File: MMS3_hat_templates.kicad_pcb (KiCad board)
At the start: 4 copper layers, 100 x 50 mm, 166 parts, among them J1 Chainbus in, J10 LED connector, J11 LED connector, J2 Chainbus Out, J3 Conn_01x04_Pin, J4 AMASS XT60 Male, J5 AMASS XT60 Female, J6 LED connector, J7 Conn_01x03_Pin, J9 Program, Q1 AO3400A, Q10 MMBT2222A 1P, Q11 MMBT2222A 1P, Q12 MMBT5401 200-300, Q13 AO3400A, Q14 MMBT2222A 1P, Q15 MMBT2222A 1P, Q16 MMBT5401 200-300, Q17 AO3400A, Q18 AO3400A, Q19 MMBT2222A 1P, Q2 MMBT2222A 1P, Q20 MMBT2222A 1P, Q21 MMBT5401 200-300, Q22 MMBT2222A 1P, Q23 MMBT2222A 1P, Q24 MMBT5401 200-300, Q25 2N7002K, Q26 2N7002K, Q27 AO3400A, Q28 MMBT2222A 1P, Q29 MMBT2222A 1P, Q3 MMBT2222A 1P, Q30 MMBT5401 200-300, Q31 AO3400A, Q32 AO3400A, Q33 MMBT2222A 1P, Q34 MMBT2222A 1P, Q35 MMBT5401 200-300, Q36 MMBT2222A 1P, Q37 MMBT2222A 1P, Q38 MMBT5401 200-300, Q4 MMBT5401 200-300, Q5 AO3400A, Q6 AO3400A, Q7 MMBT2222A 1P, Q8 MMBT2222A 1P, Q9 MMBT5401 200-300, U1 AMS1117, U2 SN74CB3Q3384APW, U3 M24C64, U4 PCA9685PW,118, U6 LM2596HVS-ADJRG, U7 CH32V003FxPx, X1 X322525MOB4SI

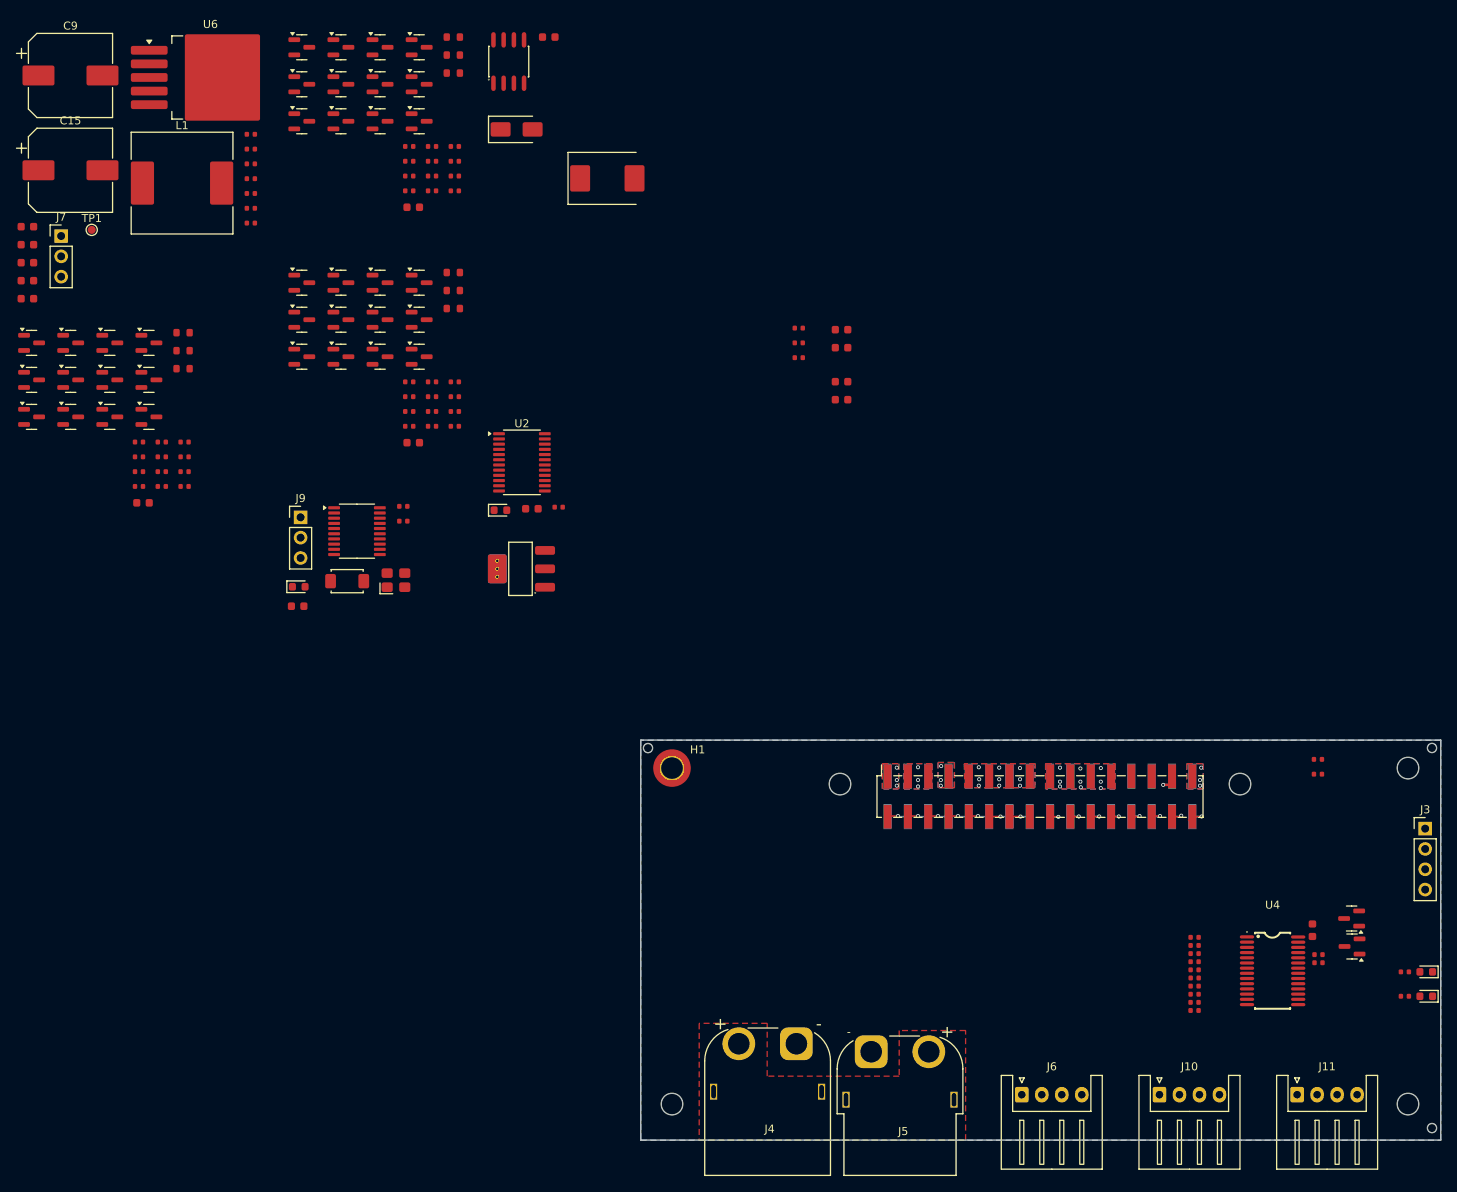
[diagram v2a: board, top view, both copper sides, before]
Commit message: PCB design
Hat allows to connect 1 LED tape at a time
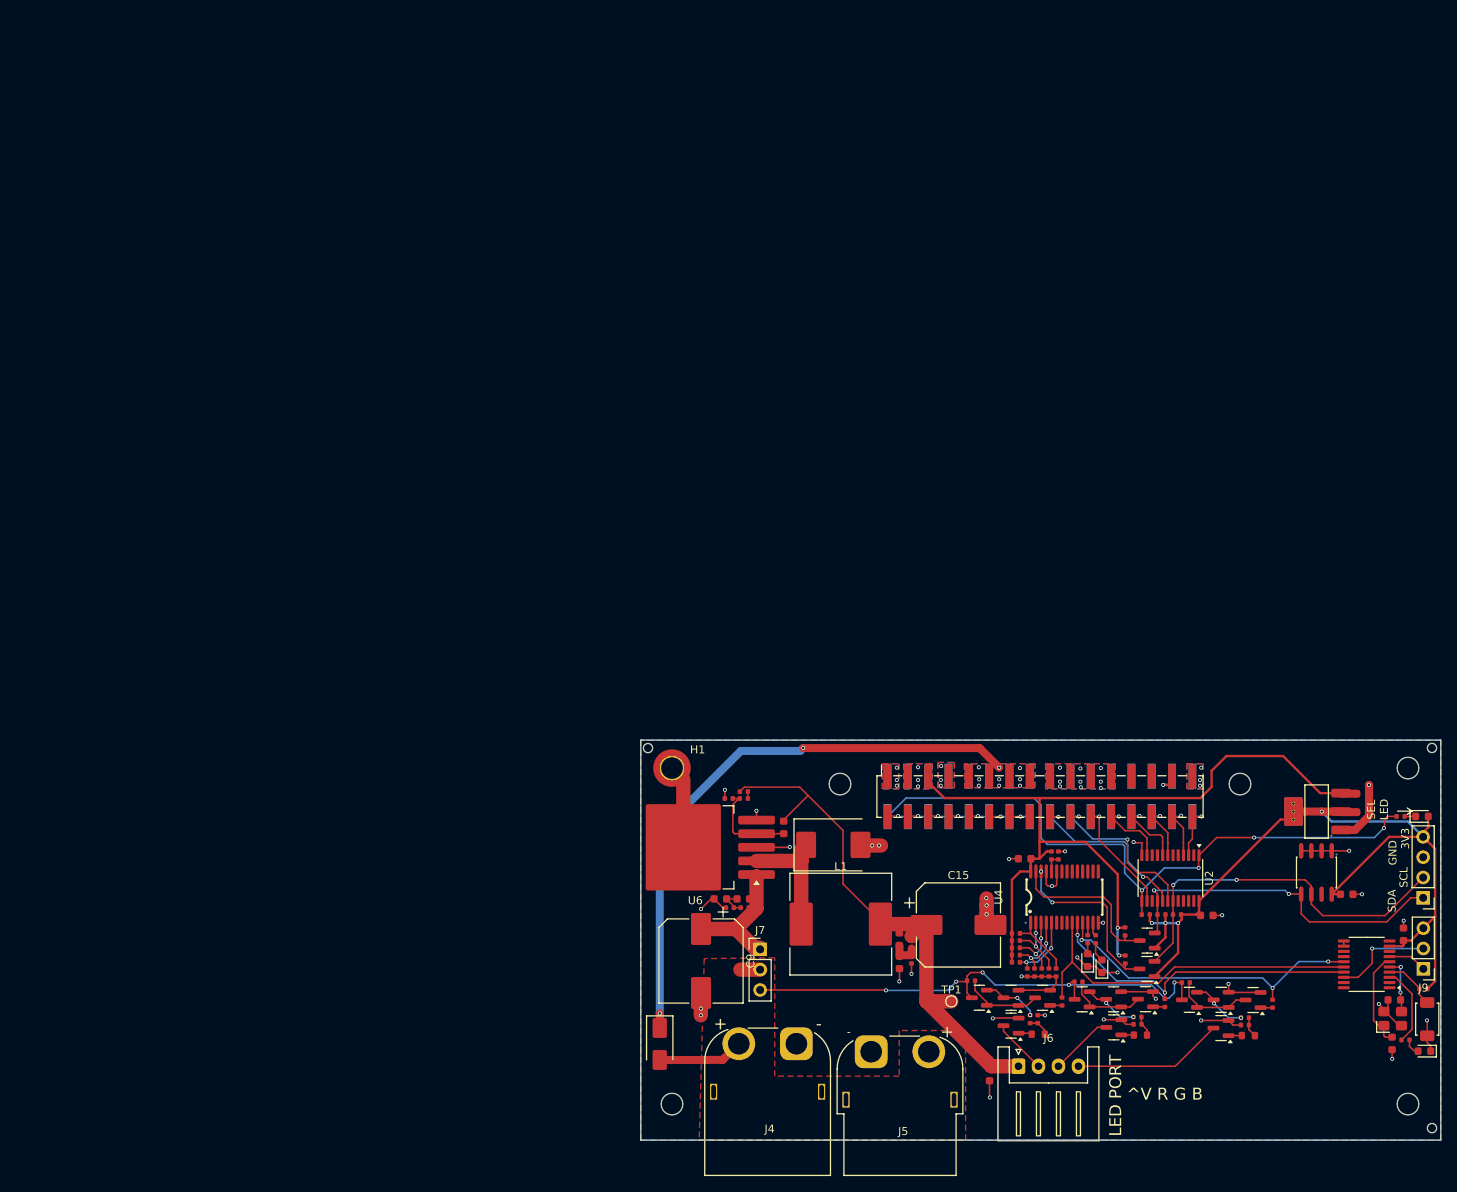
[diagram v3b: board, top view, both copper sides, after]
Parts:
- removed C19, C20: 100nF, PCM_JLCPCB:C_0603
- removed J10, J11: LED connector, Connector_JST:JST_XH_S4B-XH-A_1x04_P2.50mm_Horizontal
- removed Q14, Q15, Q19, Q20, Q22, Q23, Q28, Q29, Q33, Q34, Q36, Q37: MMBT2222A 1P, PCM_JLCPCB:Q_SOT-23
- removed Q16, Q21, Q24, Q30, Q35, Q38: MMBT5401 200-300, PCM_JLCPCB:Q_SOT-23
- removed Q17, Q18, Q31, Q32, Q5, Q6: AO3400A, PCM_JLCPCB:Q_SOT-23
- removed R34, R55, R58, R75, R78, R81: 100Ω, PCM_JLCPCB:R_0603
- removed R35, R53, R59, R73, R79, R82: 10kΩ, PCM_JLCPCB:R_0402
- removed R54, R63, R67, R74, R83, R87: 1kΩ, PCM_JLCPCB:R_0402
- removed R57, R65, R69, R77, R85, R89: 330Ω, PCM_JLCPCB:R_0402
- removed R60, R66, R70, R80, R86, R90: 47Ω, PCM_JLCPCB:R_0402
- moved Q10 158.2 mm to (154.6, 121.0), turned to 180 degrees
- moved R61 156.1 mm to (154.1, 125.4), turned to 180 degrees
- moved Q12 155.7 mm to (150.6, 121.0), turned to 180 degrees
- moved Q7 152.3 mm to (141.2, 120.9), turned to 180 degrees
- moved D9 152.2 mm to (176.0, 127.4), turned to 180 degrees
- moved Q27 151.3 mm to (150.6, 124.5), turned to 180 degrees
- moved J9 151.3 mm to (175.9, 117.1), turned to 180 degrees
- moved Q1 151.1 mm to (124.4, 124.2), turned to 180 degrees
- moved Q9 150.2 mm to (137.2, 120.9), turned to 180 degrees
- moved R31 149.6 mm to (140.6, 125.4), turned to 180 degrees
- moved Q11 149.3 mm to (146.7, 121.0), turned to 180 degrees
- moved R40 148.1 mm to (157.1, 121.5), turned to -90 degrees
- moved Q2 147.0 mm to (128.3, 120.7), turned to 180 degrees
- moved Q13 146.4 mm to (137.2, 124.4), turned to 180 degrees
- moved C4 146.4 mm to (166.3, 107.8)
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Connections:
- C12 pad 2: /12V -> U_reg
- C13 pad 1: /12V -> U_reg
- C15 pad 1: /12V -> U_reg
- J1 pad 18: /Interboard_connector/Chainbus.SDA -> /Bus_switch/Chainbus_In.SDA
- J1 pad 20: /Interboard_connector/Chainbus.SCL -> /Bus_switch/Chainbus_In.SCL
- J1 pad 22: /Interboard_connector/Chainbus.CS -> /Bus_switch/Chainbus_In.CS
- J1 pad 24: /Interboard_connector/Chainbus.SCK -> /Bus_switch/Chainbus_In.SCK
- J1 pad 26: /Interboard_connector/Chainbus.MOSI -> /Bus_switch/Chainbus_In.MOSI
- J1 pad 28: /Interboard_connector/Chainbus.MISO -> /Bus_switch/Chainbus_In.MISO
- J1 pad 30: /Interboard_connector/Chainbus.TX -> /Bus_switch/Chainbus_In.TX
- J1 pad 32: /Interboard_connector/Chainbus.RX -> /Bus_switch/Chainbus_In.RX
- J2 pad 18: /Interboard_connector/Chainbus.SDA -> /Bus_switch/Chainbus_In.SDA
- J2 pad 20: /Interboard_connector/Chainbus.SCL -> /Bus_switch/Chainbus_In.SCL
- J2 pad 22: /Interboard_connector/Chainbus.CS -> /Bus_switch/Chainbus_In.CS
- J2 pad 24: /Interboard_connector/Chainbus.SCK -> /Bus_switch/Chainbus_In.SCK
- J2 pad 26: /Interboard_connector/Chainbus.MOSI -> /Bus_switch/Chainbus_In.MOSI
- J2 pad 28: /Interboard_connector/Chainbus.MISO -> /Bus_switch/Chainbus_In.MISO
- J2 pad 30: /Interboard_connector/Chainbus.TX -> /Bus_switch/Chainbus_In.TX
- J2 pad 32: /Interboard_connector/Chainbus.RX -> /Bus_switch/Chainbus_In.RX
- L1 pad 2: /12V -> U_reg
- Q25 pad 2: /LED_IC/Chainbus.SCL -> /Bus_switch/Chainbus.SCL
- Q26 pad 2: /LED_IC/Chainbus.SDA -> /Bus_switch/Chainbus.SDA
- R48 pad 2: /12V -> U_reg
- R49 pad 1: /12V -> U_reg
- TP1 pad 1: /12V -> U_reg
- U3 pad 5: /ID EEPROM/Chainbus.SDA -> /Bus_switch/Chainbus.SDA
- U3 pad 6: /ID EEPROM/Chainbus.SCL -> /Bus_switch/Chainbus.SCL
- U4 pad 12: /R3 -> /LED_IC/S15
- U4 pad 13: /G3 -> /LED_IC/S16
- U4 pad 15: /B3 -> /LED_IC/LED8
- U4 pad 6: /R1 -> /LED_IC/LED0
- U4 pad 7: /G1 -> /LED_IC/LED1
- U4 pad 8: /B1 -> /LED_IC/LED2
- U7 pad 12: /Chainbus.SCL -> /Chainbus.SDA
- U7 pad 13: /R3 -> /CH32V003/PC3
- U7 pad 14: /G3 -> /CH32V003/PC4
- U7 pad 15: /B3 -> /B2
- U7 pad 8: /B2 -> /CH32V003/PD0
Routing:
- net GND: track 0.00 -> 116.4 mm, vias 18 -> 54
- net +5V: track 0.69 -> 109.0 mm, vias 3 -> 5
- net +3V3: track 0.00 -> 106.0 mm, vias 0 -> 4
- net /Bus_switch/SEL1: track 0.00 -> 82.1 mm, vias 0 -> 4
- net VIN_CHAINBUS: track 0.76 -> 73.0 mm, vias 9 -> 11
- net U_reg: track 0.00 -> 67.7 mm
- net /12V: track 0.00 -> 64.5 mm, vias 0 -> 5
- net /Bus_switch/Chainbus.SCL: track 0.00 -> 47.2 mm, vias 0 -> 2
- net /R2: track 0.00 -> 45.7 mm
- net /Bus_switch/Chainbus.SDA: track 0.00 -> 44.5 mm, vias 0 -> 2
- net /G2: track 0.00 -> 41.0 mm, vias 0 -> 2
- net /B2: track 0.00 -> 40.3 mm, vias 0 -> 3
- net /LED_IC/SCL_5V: track 0.00 -> 22.6 mm, vias 0 -> 2
- net /Bus_switch/Chainbus_In.SDA: track 0.00 -> 22.3 mm, vias 0 -> 2
- net /Bus_switch/Chainbus_In.SCL: track 0.00 -> 21.6 mm, vias 0 -> 2
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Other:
- board text added: "3V3"
- board text added: "GND"
- board text added: "LED PORT"
- board text added: "LED TAPE CONTROLLER HAT"
- board text added: "PWM CONTROLLER SETUP"
- board text added: "SCL"
- board text added: "SDA"
- board text added: "SEL LED"
- board text added: "^V R G B"
- board text added: "uC SETUP"

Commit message: PCB addjustments
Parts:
- added D10: SS510C, PCM_JLCPCB:D_SMC, F.Cu at (114.7, 119.6)
- added D8: SS510C, PCM_JLCPCB:D_SMC, F.Cu at (101.7, 120.2)
- moved TP1 5.40 mm to (119.0, 116.2)
- moved C15 3.84 mm to (118.0, 107.8)
- moved C13 3.51 mm to (110.3, 109.9)
- moved C14 3.51 mm to (110.4, 112.8)
- moved R49 3.51 mm to (111.9, 110.5)
- moved R50 3.51 mm to (111.9, 112.4)
- moved D6 1.25 mm to (102.1, 100.4)
- moved L1 1.23 mm to (102.9, 110.3)
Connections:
- C12 pad 2: U_reg -> Net-(C12-Pad2)
- C13 pad 1: U_reg -> Net-(C12-Pad2)
- C15 pad 1: U_reg -> Net-(C12-Pad2)
- C6 pad 1: U_reg -> /12V
- J6 pad 1: U_reg -> /12V
- J7 pad 3: /12V -> Net-(J7-Pin_3)
- L1 pad 2: U_reg -> Net-(C12-Pad2)
- R48 pad 2: U_reg -> Net-(C12-Pad2)
- R49 pad 1: U_reg -> Net-(C12-Pad2)
- TP1 pad 1: U_reg -> Net-(C12-Pad2)
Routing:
- net U_reg: track 67.7 -> 0.00 mm
- net Net-(C12-Pad2): track 0.00 -> 53.0 mm
- net /12V: track 64.5 -> 79.6 mm
- net Net-(J7-Pin_3): track 0.00 -> 5.47 mm
- net /Buck Regulator/sw: track 16.0 -> 17.2 mm
